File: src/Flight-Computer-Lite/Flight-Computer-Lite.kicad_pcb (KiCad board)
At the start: 4 copper layers, 85.8 x 30 mm, 76 parts, among them J1 Jumper_NO, J2 Jumper_NO, P1 1546551-2, P2 3220-20-0200-00, P3 USB, P4 1984659, Q1 QS5U17TR, Q2 QS5U17TR, U1 STM32H750VBTx, U2 LMS8117AMP-3.3_NOPB, U3 SST25VF040B-50-4I-S2AE-T, U4 CP2102-GMR(QFN28), U5 TS391IYLT, U6 BMP390, U7 TS391IYLT, U8 TS391IYLT, Y1 ECS-240-18-33-JGN-TR

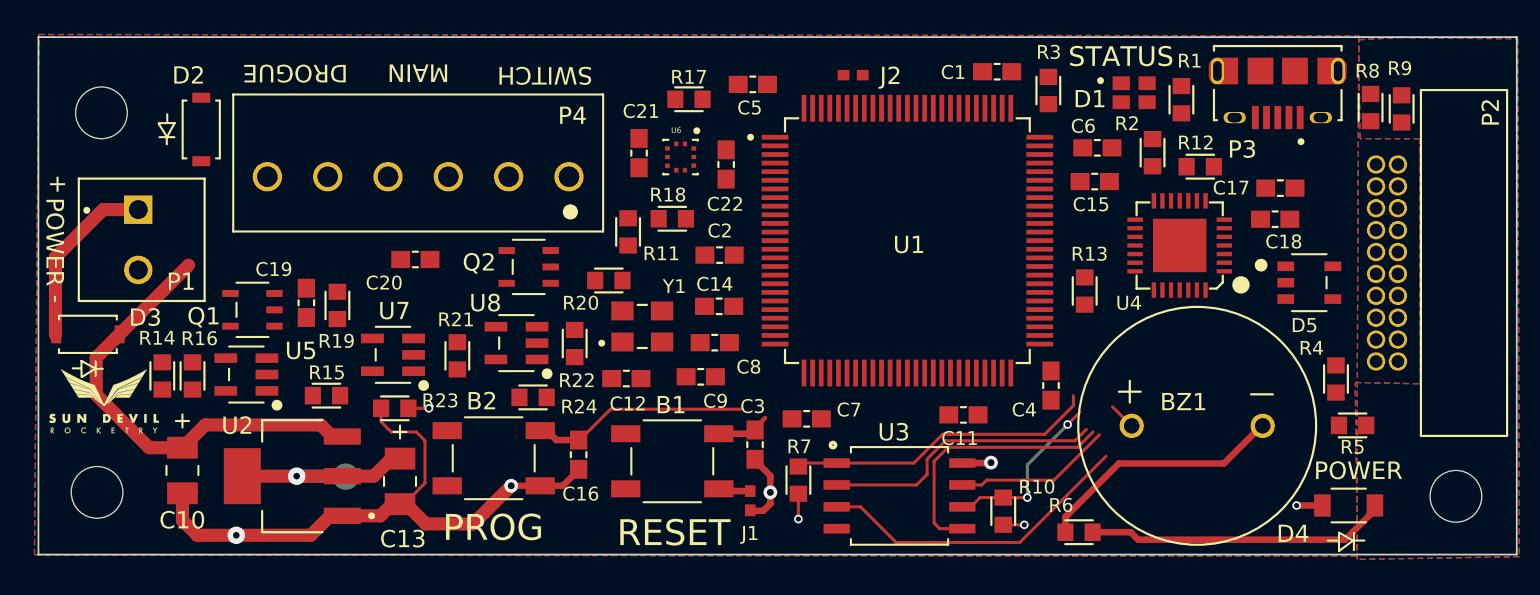
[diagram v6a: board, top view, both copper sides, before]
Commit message: re-routed PCB to smaller form factor
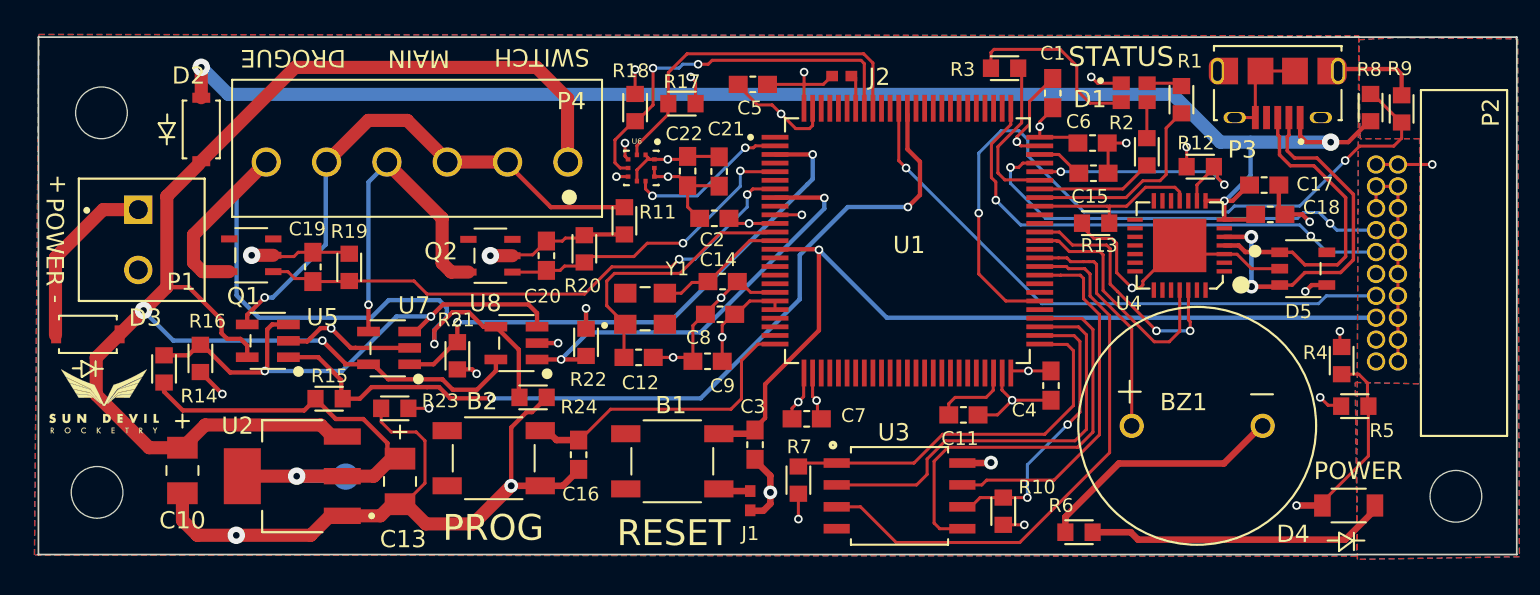
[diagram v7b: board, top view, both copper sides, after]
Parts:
- moved C20 7.61 mm to (180.3, 93.0), turned to 90 degrees
- moved R18 6.80 mm to (185.4, 84.5), turned to 90 degrees
- moved C21 4.77 mm to (190.3, 88.2)
- moved R13 3.99 mm to (212.2, 91.2), turned to 0 degrees
- moved C1 3.46 mm to (209.7, 83.6), turned to 90 degrees
- moved Q1 3.17 mm to (163.2, 93.0)
- moved R3 2.85 mm to (206.9, 82.2), turned to 180 degrees
- moved U6 2.37 mm to (185.9, 88.0)
- moved R20 2.32 mm to (182.5, 92.7), turned to -90 degrees
- moved U5 2.32 mm to (164.1, 98.0)
- moved Q2 2.32 mm to (177.1, 93.0)
- moved R19 2.31 mm to (168.9, 93.7)
- moved C22 2.27 mm to (188.5, 88.1), turned to -90 degrees
- moved C2 2.16 mm to (190.0, 90.9)
- moved C19 2.12 mm to (166.8, 93.7)
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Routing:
- net Earth: track 53.0 -> 163.0 mm, vias 4 -> 22
- net 5V: track 0.00 -> 93.5 mm, vias 0 -> 4
- net 3.3V: track 16.1 -> 80.6 mm, vias 4 -> 18
- net VIN: track 25.2 -> 89.5 mm, vias 0 -> 2
- net ~{SWITCH}: track 0.00 -> 50.1 mm, vias 0 -> 2
- net NRST: track 2.54 -> 50.1 mm, vias 0 -> 1
- net Net-(P4-Pad6): track 0.00 -> 43.6 mm, vias 0 -> 1
- net USB_DETECT: track 0.00 -> 43.5 mm, vias 0 -> 2
- net SWCLK: track 0.00 -> 40.1 mm, vias 0 -> 3
- net SWO: track 0.00 -> 34.4 mm, vias 0 -> 1
- net SWDIO: track 0.00 -> 32.2 mm, vias 0 -> 3
- net VIN_SW: track 0.00 -> 31.9 mm, vias 0 -> 1
- net DROGUE: track 0.00 -> 31.9 mm, vias 0 -> 2
- net ~{MAIN_CONT}: track 0.00 -> 31.8 mm, vias 0 -> 2
- net VCOMP: track 0.00 -> 29.3 mm, vias 0 -> 2
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
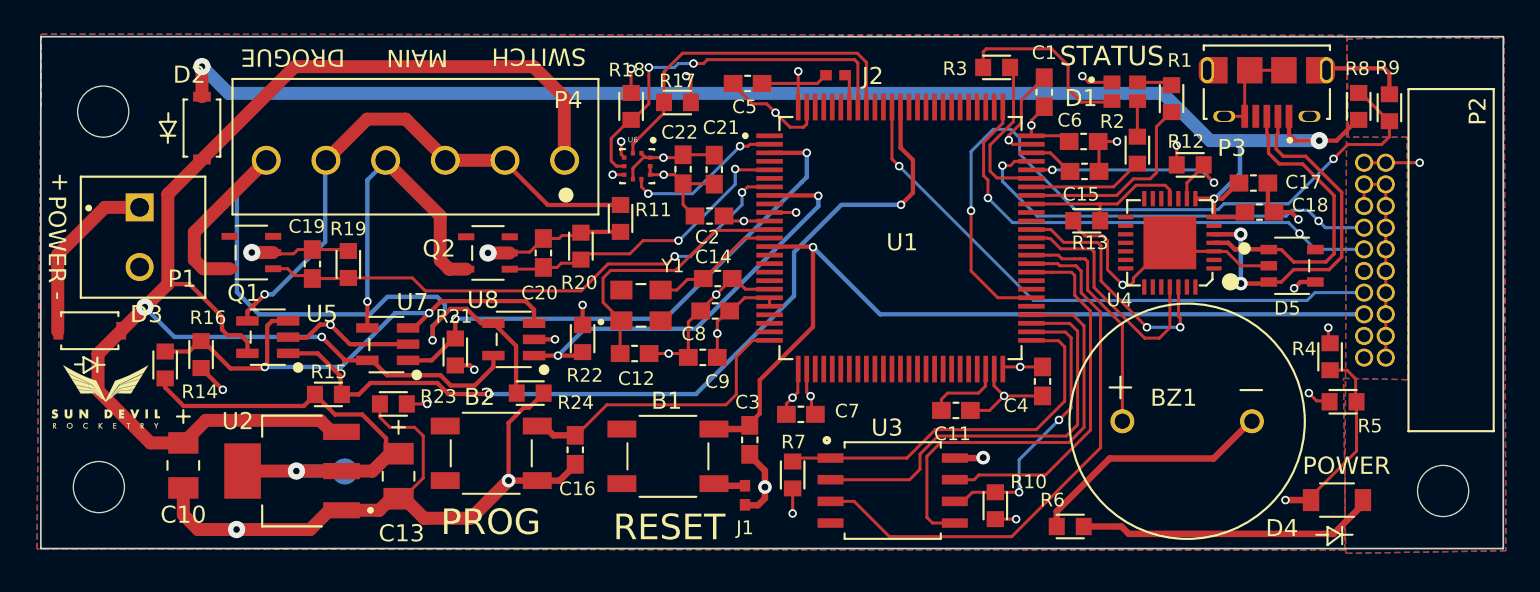
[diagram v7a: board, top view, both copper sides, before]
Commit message: placed rev2 components on board
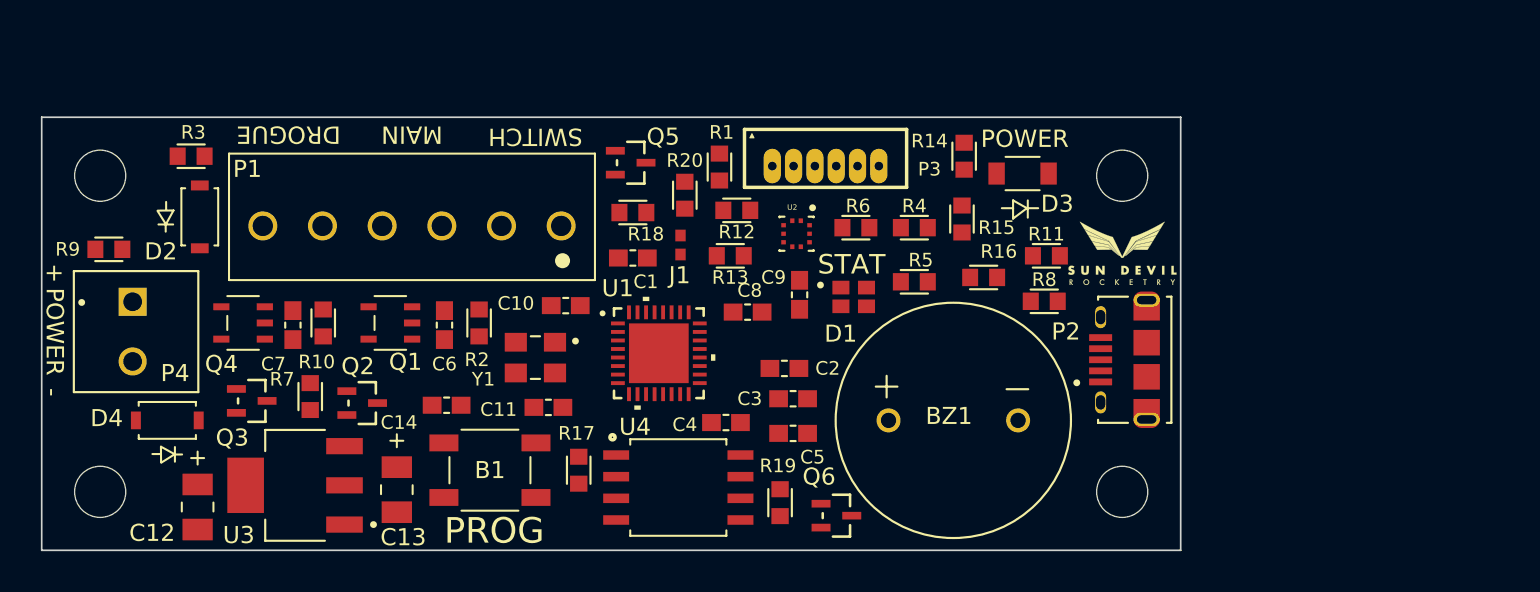
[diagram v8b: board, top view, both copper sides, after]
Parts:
- removed B2: PTS647SM38SMTR2LFS, Flight-Computer-Lite:PTS647SM38SMTR2LFS
- removed the C11 at (204.5, 102.3)
- removed C15: 2.2uF, Flight-Computer-Lite:CAP_0603
- removed C16, C18, C21, C22: 0.1uF, Flight-Computer-Lite:CAP_0603
- removed C17, C19, C20: 1uF, Flight-Computer-Lite:CAP_0603
- removed the C3 at (192.4, 104.0)
- removed the C5 at (192.3, 83.1)
- removed D5: SP0504BAHTG, Flight-Computer-Lite:SP0504BAHTG
- removed the J1 at (192.1, 107.3)
- removed the P4 at (181.5, 87.6)
- removed the R14 at (158.1, 99.6)
- removed the R15 at (167.7, 101.3)
- removed the R16 at (160.2, 99.0)
- removed R21, R22, R23, R24: 10k, Flight-Computer-Lite:RES_0603
- removed TP1: TP, Flight-Computer-Lite:TP
- removed the U3 at (200.8, 107.0)
- removed U5, U7, U8: TS391IYLT, Flight-Computer:TS391IYLT
- removed U6: BMP390, Flight-Computer-Lite:BMP390
- added C14: 0.1uF, Flight-Computer-Lite:CAP_0603, F.Cu at (174.6, 102.0)
- added C8: 0.1uF, Flight-Computer-Lite:CAP_0603, F.Cu at (192.3, 96.5)
- added C9: 0.1uF, Flight-Computer-Lite:CAP_0603, F.Cu at (195.3, 95.5)
- added H1: Mounting-Hole, Flight-Computer-Lite:MountingHole_3mm, F.Cu at (214.2, 88.5)
- added P1: CONN_1984659_PXC, Flight-Computer-Lite:1984659, F.Cu at (181.3, 91.5)
- added Q3: 2N7002W-7-F, Flight-Computer-Lite:2N7002W-7-F, F.Cu at (163.2, 101.7)
- added Q4: QS5U17TR, Flight-Computer-Lite:QS5U17TR, F.Cu at (162.7, 97.2)
- added Q5: 2N7002W-7-F, Flight-Computer-Lite:2N7002W-7-F, F.Cu at (185.4, 87.8)
- added Q6: 2N7002W-7-F, Flight-Computer-Lite:2N7002W-7-F, F.Cu at (197.5, 108.5)
- added R1: 10k, Flight-Computer-Lite:RES_0603, F.Cu at (190.6, 88.0)
- added R2: 100k, Flight-Computer-Lite:RES_0603, F.Cu at (176.5, 97.2)
- added R3: 10k, Flight-Computer-Lite:RES_0603, F.Cu at (159.6, 87.4)
- added U2: BMP390, Flight-Computer-Lite:BMP390, F.Cu at (195.2, 91.9)
- B1: footprint Flight-Computer:PTS647SM38SMTR2LFS -> Flight-Computer-Lite:PTS647SM38SMTR2LFS
- C4: renamed from C8; value 0.1uF -> 0.01uF
- C6, C7: value 0.1uF -> 1uF
- P2: value 3220-20-0200-00 -> USB; footprint Flight-Computer-Lite:3220-20-0200-00 -> Flight-Computer-Lite:10118194-0001LF
- P3: value USB -> 0530470610; footprint Flight-Computer-Lite:10118194-0001LF -> Flight-Computer-Lite:53047-0610
- Q2: value QS5U17TR -> 2N7002W-7-F; footprint Flight-Computer-Lite:QS5U17TR -> Flight-Computer-Lite:2N7002W-7-F
- R10: value 10k -> 100k
- R11: value 10k -> 20k
- R13: value 10k -> 4.7k
- R17, R18: value 4.7k -> 10k
- R19, R20: value 100k -> 10k
- R9: value 20k -> 10k
- U1: value STM32H750VBTx -> STM32G4A1KEU6; footprint Flight-Computer-Lite:STM32H750VBT6 -> Flight-Computer-Lite:STM32G4A1KEU6
- U4: value CP2102-GMR(QFN28) -> SST25VF040B-50-4I-S2AE-T; footprint Flight-Computer-Lite:CP2012-GMR -> Flight-Computer-Lite:SST25VF040B-50-4I-S2AE-T
- moved R9 75.6 mm to (154.8, 92.8), turned to 0 degrees
- moved LOGO1 60.2 mm to (214.2, 93.0)
- moved R10 40.9 mm to (167.4, 97.2), turned to -90 degrees
- moved C6 39.0 mm to (174.5, 97.3), turned to -90 degrees
- moved U4 32.2 mm to (188.2, 106.8), turned to 0 degrees
- moved C7 30.3 mm to (165.6, 97.3), turned to 90 degrees
- moved R19 28.9 mm to (194.2, 107.7), turned to 90 degrees
- moved R7 28.7 mm to (166.6, 101.5)
- moved R12 26.7 mm to (191.6, 90.6), turned to 180 degrees
- moved D3 26.6 mm to (208.4, 88.4)
- moved P3 26.5 mm to (196.8, 88.0)
- moved R11 25.1 mm to (209.8, 93.2), turned to 0 degrees
- moved R15 24.8 mm to (204.9, 91.1), turned to -90 degrees
- moved R14 24.5 mm to (205.0, 87.4)
- moved C3 23.2 mm to (194.9, 101.6), turned to 0 degrees
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- renumbered C2 to C1, C12 to C10, C14 to C11, C10 to C12, C4 to C2, C1 to C3, C9 to C5, D4 to D3, D3 to D4, H1 to H2, H4 to H3, H3 to H4, J2 to J1, P1 to P4, R4 to R14, R5 to R15, R6 to R16, R1 to R4, R2 to R5, R3 to R6, U2 to U3
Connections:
- net /PIN_SCREW renamed Net-(D4-Pad2)
- B1 pad 1: Net-(B1-Pad1) -> Earth
- B1 pad 3: NRST -> PROG
- BZ1 pad 1: BEEP -> VIN
- BZ1 pad 2: Earth -> Net-(BZ1-Pad2)
- C6 pad 1: 3.3V -> MAIN
- C7 pad 1: 3.3V -> DROGUE
- P2 pad 1: 3.3V -> 5V
- P2 pad 2: 3.3V -> USB_D-
- P2 pad 3: Earth -> USB_D+
- P2 pad 4: Earth -> unconnected-(P2-Pad4)
- P3 pad 1: 5V -> 3.3V
- P3 pad 2: /Peripherals/D- -> SWDIO
- P3 pad 3: /Peripherals/D+ -> SWCLK
- P3 pad 4: unconnected-(P3-Pad4) -> SWO
- P3 pad 5: Earth -> NRST
- Q1 pad 1: DROGUE -> MAIN
- Q1 pad 5: Net-(P4-Pad6) -> Net-(P1-Pad4)
- Q2 pad 1: MAIN -> Net-(P1-Pad4)
- Q2 pad 3: unconnected-(Q2-Pad3) -> ~{MAIN_CONT}
- R10 pad 2: FLASH_SCK -> DROGUE
- R11 pad 2: VIN_SW -> USB_DETECT
- R12 pad 1: 3.3V -> BP_SCL
- R12 pad 2: ~{USB_RST} -> 3.3V
- R13 pad 1: Earth -> BP_SDA
- R13 pad 2: ~{USB_SUSPEND} -> 3.3V
- R17 pad 1: BP_SCL -> ~{FLASH_SS}
- R18 pad 1: BP_SDA -> ~{SWITCH}
- R19 pad 2: DROGUE -> FLASH_SCK
- R20 pad 2: MAIN -> VIN_SW
- R7 pad 1: ~{FLASH_SS} -> ~{DROGUE_CONT}
- R9 pad 2: USB_DETECT -> Net-(P1-Pad6)
- U1 pad 1: unconnected-(U1-Pad1) -> 3.3V
- U1 pad 10: Earth -> FLASH_SCK
- U1 pad 11: 3.3V -> ~{FLASH_SS}
- U1 pad 12: OSC_IN -> FLASH_MOSI
- U1 pad 13: OSC_OUT -> FLASH_MISO
- U1 pad 14: NRST -> Earth
- U1 pad 15: unconnected-(U1-Pad15) -> 3.3V
- U1 pad 16: unconnected-(U1-Pad16) -> Earth
- U1 pad 17: unconnected-(U1-Pad17) -> 3.3V
- U1 pad 18: unconnected-(U1-Pad18) -> BP_SDA
- U1 pad 19: Earth -> BP_SCL
- U1 pad 2: BP_INT -> OSC_IN
- U1 pad 20: 3.3V -> PROG
- U1 pad 21: 3.3V -> USB_D-
- U1 pad 22: unconnected-(U1-Pad22) -> USB_D+
- U1 pad 23: unconnected-(U1-Pad23) -> SWDIO
- U1 pad 24: unconnected-(U1-Pad24) -> SWCLK
- U1 pad 25: PROG -> ~{DROGUE_CONT}
- U1 pad 26: Earth -> SWO
- U1 pad 27: 3.3V -> DROGUE
- U1 pad 28: unconnected-(U1-Pad28) -> STATUS_R
- U1 pad 29: unconnected-(U1-Pad29) -> STATUS_G
- U1 pad 3: ~{MAIN_CONT} -> OSC_OUT
- U1 pad 30: unconnected-(U1-Pad30) -> STATUS_B
- U1 pad 31: unconnected-(U1-Pad31) -> BOOT
- U1 pad 32: unconnected-(U1-Pad32) -> Earth
- U1 pad 4: unconnected-(U1-Pad4) -> NRST
- U1 pad 5: MAIN -> USB_DETECT
- U1 pad 6: unconnected-(U1-Pad6) -> ~{SWITCH}
- U1 pad 7: DROGUE -> BEEP
- U1 pad 8: ~{DROGUE_CONT} -> MAIN
- U1 pad 9: unconnected-(U1-Pad9) -> ~{MAIN_CONT}
- U4 pad 1: unconnected-(U4-Pad1) -> ~{FLASH_SS}
- U4 pad 2: unconnected-(U4-Pad2) -> FLASH_MISO
- U4 pad 3: Earth -> 3.3V
- U4 pad 4: /Peripherals/D+ -> Earth
- U4 pad 5: /Peripherals/D- -> FLASH_MOSI
- U4 pad 6: unconnected-(U4-Pad6) -> FLASH_SCK
- U4 pad 7: 5V -> 3.3V
- U4 pad 8: 5V -> 3.3V
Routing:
- net Earth: track 163.0 -> 0.00 mm, vias 22 -> 0
- net 5V: track 93.5 -> 0.00 mm, vias 4 -> 0
- net VIN: track 89.5 -> 0.00 mm, vias 2 -> 0
- net 3.3V: track 80.6 -> 0.07 mm, vias 18 -> 0
- net NRST: track 50.1 -> 0.00 mm, vias 1 -> 0
- net ~{SWITCH}: track 50.1 -> 0.00 mm, vias 2 -> 0
- net Net-(P4-Pad6): track 43.6 -> 0.00 mm, vias 1 -> 0
- net USB_DETECT: track 43.5 -> 0.00 mm, vias 2 -> 0
- net SWCLK: track 40.1 -> 0.00 mm, vias 3 -> 0
- net SWO: track 34.4 -> 0.00 mm, vias 1 -> 0
- net ~{FLASH_WP}: track 32.8 -> 0.00 mm
- net SWDIO: track 32.2 -> 0.00 mm, vias 3 -> 0
- net VIN_SW: track 31.9 -> 0.00 mm, vias 1 -> 0
- net DROGUE: track 31.9 -> 0.00 mm, vias 2 -> 0
- net ~{MAIN_CONT}: track 31.8 -> 0.00 mm, vias 2 -> 0
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- removed copper zone on In2.Cu, net 3.3V
- removed copper zone on B.Cu, net Earth
- removed copper zone on F.Cu, net Earth
- removed copper zone on In1.Cu, net Earth
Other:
- board size 85.8 x 30 mm -> 66.8 x 25.4 mm
- board text added: "A0007 Flight Computer Lite Rev 2.0"
- board text added: "STAT"
- board text removed: "A0007 Flight Computer Lite Rev 1.0"
- board text removed: "RESET"
- board text removed: "STATUS"
